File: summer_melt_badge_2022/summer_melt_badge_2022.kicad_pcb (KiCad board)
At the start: 2 copper layers, 52.4 x 98 mm, 1 part

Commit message: draft schematic for review.
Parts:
- renumbered G*** to -
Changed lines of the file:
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@@
     (at 99.06 86.36)
     (attr board_only exclude_from_pos_files exclude_from_bom)
-    (fp_text reference "G***" (at 0 0) (layer "F.SilkS")
+    (fp_text reference "-" (at -18.31 1.64 90) (layer "F.SilkS")
       (effects (font (size 1.524 1.524) (thickness 0.3)))
     )

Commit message: footprint assignment, placement started
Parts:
- added BT1: Battery, Battery:BatteryHolder_Keystone_2468_2xAAA, B.Cu at (92.7, 54.8)
- added D1: LED, LED_THT:LED_D5.0mm, F.Cu at (120.7, 66.0)
- added D2: LED, LED_THT:LED_D5.0mm, F.Cu at (116.8, 57.1)
- added D3: LED, LED_THT:LED_D5.0mm, F.Cu at (86.4, 57.1)
- added D4: LED, LED_THT:LED_D5.0mm, F.Cu at (119.4, 76.2)
- added D5: LED, LED_THT:LED_D5.0mm, F.Cu at (111.8, 48.3)
- added D6: LED, LED_THT:LED_D5.0mm, F.Cu at (96.5, 50.8)
- added H1: MountingHole, lanyard_slot:lanyard_slot, F.Cu at (106.7, 45.7)
- added J1: Conn_02x03_Odd_Even, Connector_PinSocket_2.54mm:PinSocket_2x03_P2.54mm_Vertical, F.Cu at (83.8, 121.9)
- added R1: 4.7k, Resistor_THT:R_Axial_Power_L25.0mm_W9.0mm_P30.48mm, F.Cu at (128.3, 102.9)
- added S1: SS12D07VG4, SS12D07VG4:SW_SS12D07VG4, F.Cu at (83.8, 78.7)
- added U1: WeMos_D1_mini, Module:WEMOS_D1_mini_light, F.Cu at (80.5, 87.6)
- added U2: DS18B20, Package_TO_SOT_THT:TO-92_Inline, F.Cu at (87.6, 118.1)

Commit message: draft placement complete.
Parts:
- added G***: LOGO, summer_melt_badge_2022:summer_melt_cone_logo, F.Cu at (183.9, 95.7)
- R1: footprint Resistor_THT:R_Axial_Power_L25.0mm_W9.0mm_P30.48mm -> Resistor_THT:R_Axial_DIN0207_L6.3mm_D2.5mm_P10.16mm_Horizontal
- U1: moved to B.Cu
- moved D5 56.1 mm to (119.4, 103.9), turned to 60 degrees
- moved R1 50.7 mm to (81.9, 82.5), turned to -40 degrees
- moved D4 41.3 mm to (119.2, 117.5)
- moved D6 34.5 mm to (127.2, 66.5)
- moved D3 34.5 mm to (119.6, 48.1), turned to 30 degrees
- moved U2 24.5 mm to (81.2, 94.5), turned to 50 degrees
- moved D2 23.3 mm to (128.2, 77.5)
- moved U1 21.5 mm to (78.2, 109.0), turned to -40 degrees
- moved J1 20.7 mm to (78.5, 142.0)
- moved BT1 17.3 mm to (78.9, 65.3), turned to -40 degrees
- moved S1 8.69 mm to (76.2, 83.0), turned to -100 degrees
- moved H1 8.45 mm to (111.8, 39.0), turned to -20 degrees
- moved D1 7.85 mm to (122.7, 58.5), turned to 10 degrees
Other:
- board size 52.4 x 98 mm -> 64.1 x 119.8 mm
- board text added: "SCALE UP SILKSC ARTWORK"

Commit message: final draft placement
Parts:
- removed -: LOGO, summer_melt_badge_2022:summer_melt_cone_logo
- removed D3: LED, LED_THT:LED_D5.0mm
- removed the G*** at (183.9, 95.7)
- added G***: LOGO, summer_melt_badge_2022:summer_melt_cone_logo78, F.Cu at (98.9, 91.0)
- moved D6 39.0 mm to (93.9, 46.1)
- moved U1 28.7 mm to (107.0, 109.5), turned to 145 degrees
- moved D1 11.8 mm to (115.4, 49.3), turned to 110 degrees
- moved D2 9.52 mm to (126.6, 68.1), turned to -40 degrees
- moved D5 3.43 mm to (119.3, 100.4)
- moved BT1 0.57 mm to (78.6, 65.8), turned to -30 degrees

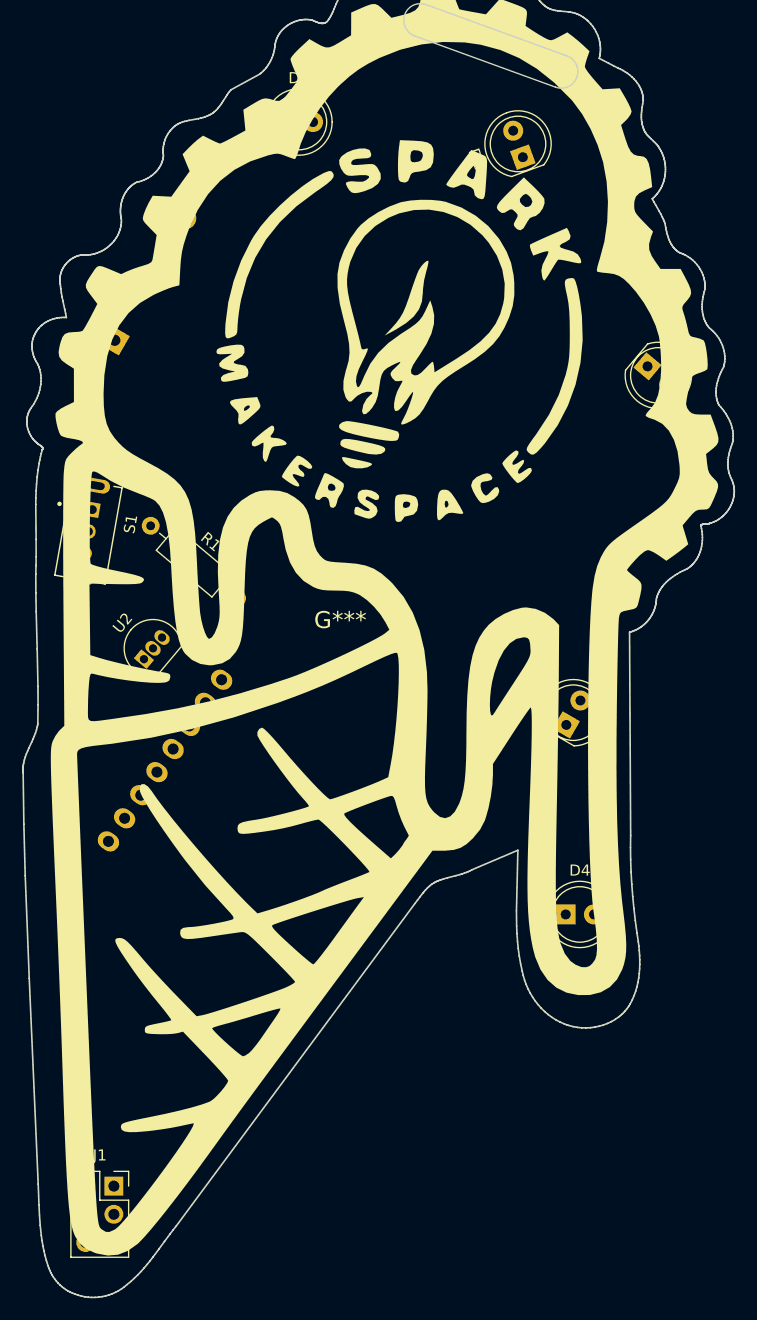
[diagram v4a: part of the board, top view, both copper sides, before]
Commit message: Minor edits during final placement review
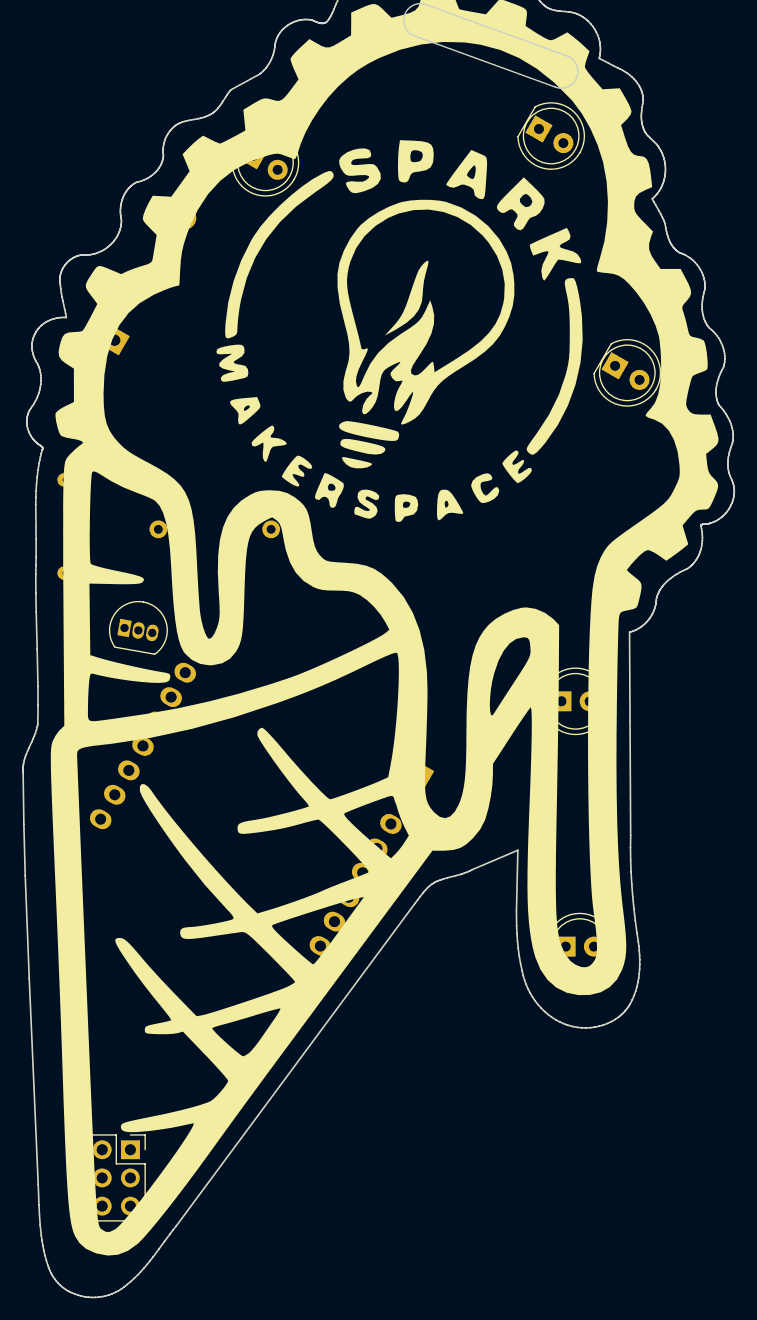
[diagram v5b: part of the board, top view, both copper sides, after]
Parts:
- R1, S1: moved to B.Cu
- moved R1 10.9 mm to (92.7, 82.8), turned to 180 degrees
- moved U1 4.61 mm to (106.0, 105.0), turned to 150 degrees
- moved D5 4.16 mm to (91.1, 49.1), turned to -30 degrees
- moved J1 3.60 mm to (80.0, 138.7)
- moved U2 3.31 mm to (79.5, 91.7), turned to -10 degrees
- moved D1 2.93 mm to (116.8, 46.7), turned to -30 degrees
- moved D2 2.92 mm to (123.7, 68.1), turned to -30 degrees
- moved D3 2.90 mm to (119.2, 120.4)
- moved D4 2.17 mm to (118.9, 98.3), turned to 0 degrees
- moved S1 1.64 mm to (74.7, 82.5), turned to -90 degrees
- renumbered D4 to D3, D5 to D4, D6 to D5
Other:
- board text added: "Important! Do not power with USB and Battery at the same time!"

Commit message: draft traces
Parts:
- moved R1 0.85 mm to (92.1, 83.4)
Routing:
- net GND: track 0.00 -> 211.2 mm, vias 0 -> 3
- net GPIO0: track 0.00 -> 134.8 mm, vias 0 -> 5
- net Net-(D5-Pad2): track 0.00 -> 112.5 mm, vias 0 -> 7
- net +3V0: track 0.00 -> 105.4 mm, vias 0 -> 4
- net Net-(D1-Pad2): track 0.00 -> 70.8 mm, vias 0 -> 2
- net Net-(D4-Pad2): track 0.00 -> 52.0 mm, vias 0 -> 4
- net Net-(D3-Pad2): track 0.00 -> 51.1 mm, vias 0 -> 4
- net SDA: track 0.00 -> 49.4 mm, vias 0 -> 2
- net SCL: track 0.00 -> 45.3 mm
- net GPIO1: track 0.00 -> 42.6 mm, vias 0 -> 1
- net DQ: track 0.00 -> 19.6 mm
- net +BATT: track 0.00 -> 16.4 mm
- added copper zone on B.Cu, net GND
- added copper zone on F.Cu, net GND
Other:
- board text removed: "SCALE UP SILKSC ARTWORK"

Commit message: routed board review complete
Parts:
- moved H1 1.14 mm to (111.8, 40.1)
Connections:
- J1 pad 1: GND -> +3V0
- J1 pad 2: +3V0 -> GND
- J1 pad 3: SCL -> SDA
- J1 pad 4: SDA -> SCL
- J1 pad 5: GPIO1 -> GPIO0
- J1 pad 6: GPIO0 -> GPIO1
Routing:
- net GND: track 211.2 -> 26.0 mm, vias 3 -> 1
- net Net-(D4-Pad2): track 52.0 -> 29.0 mm, vias 4 -> 0
- net Net-(D3-Pad2): track 51.1 -> 31.8 mm, vias 4 -> 0
- net GPIO1: track 42.6 -> 56.5 mm
- net SDA: track 49.4 -> 42.7 mm, vias 2 -> 0
- net Net-(D5-Pad2): track 112.5 -> 107.2 mm, vias 7 -> 3
- net SCL: track 45.3 -> 50.6 mm, vias 0 -> 1
- net DQ: track 19.6 -> 19.0 mm
- net GPIO0: track 134.8 -> 134.4 mm, vias 5 -> 3
- net +3V0: track 105.4 -> 105.1 mm, vias 4 -> 2
- removed copper zone on B.Cu, net GND
